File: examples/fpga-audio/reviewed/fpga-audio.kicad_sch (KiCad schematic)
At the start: 36 parts, among them J1 3V3 IN, J2 AUDIO OUT, J3 SPI PROG, U1 iCE40UP5K, U2 PCM5102A, U3 AP2112K-1.2, U4 W25Q32JV, X1 12MHz

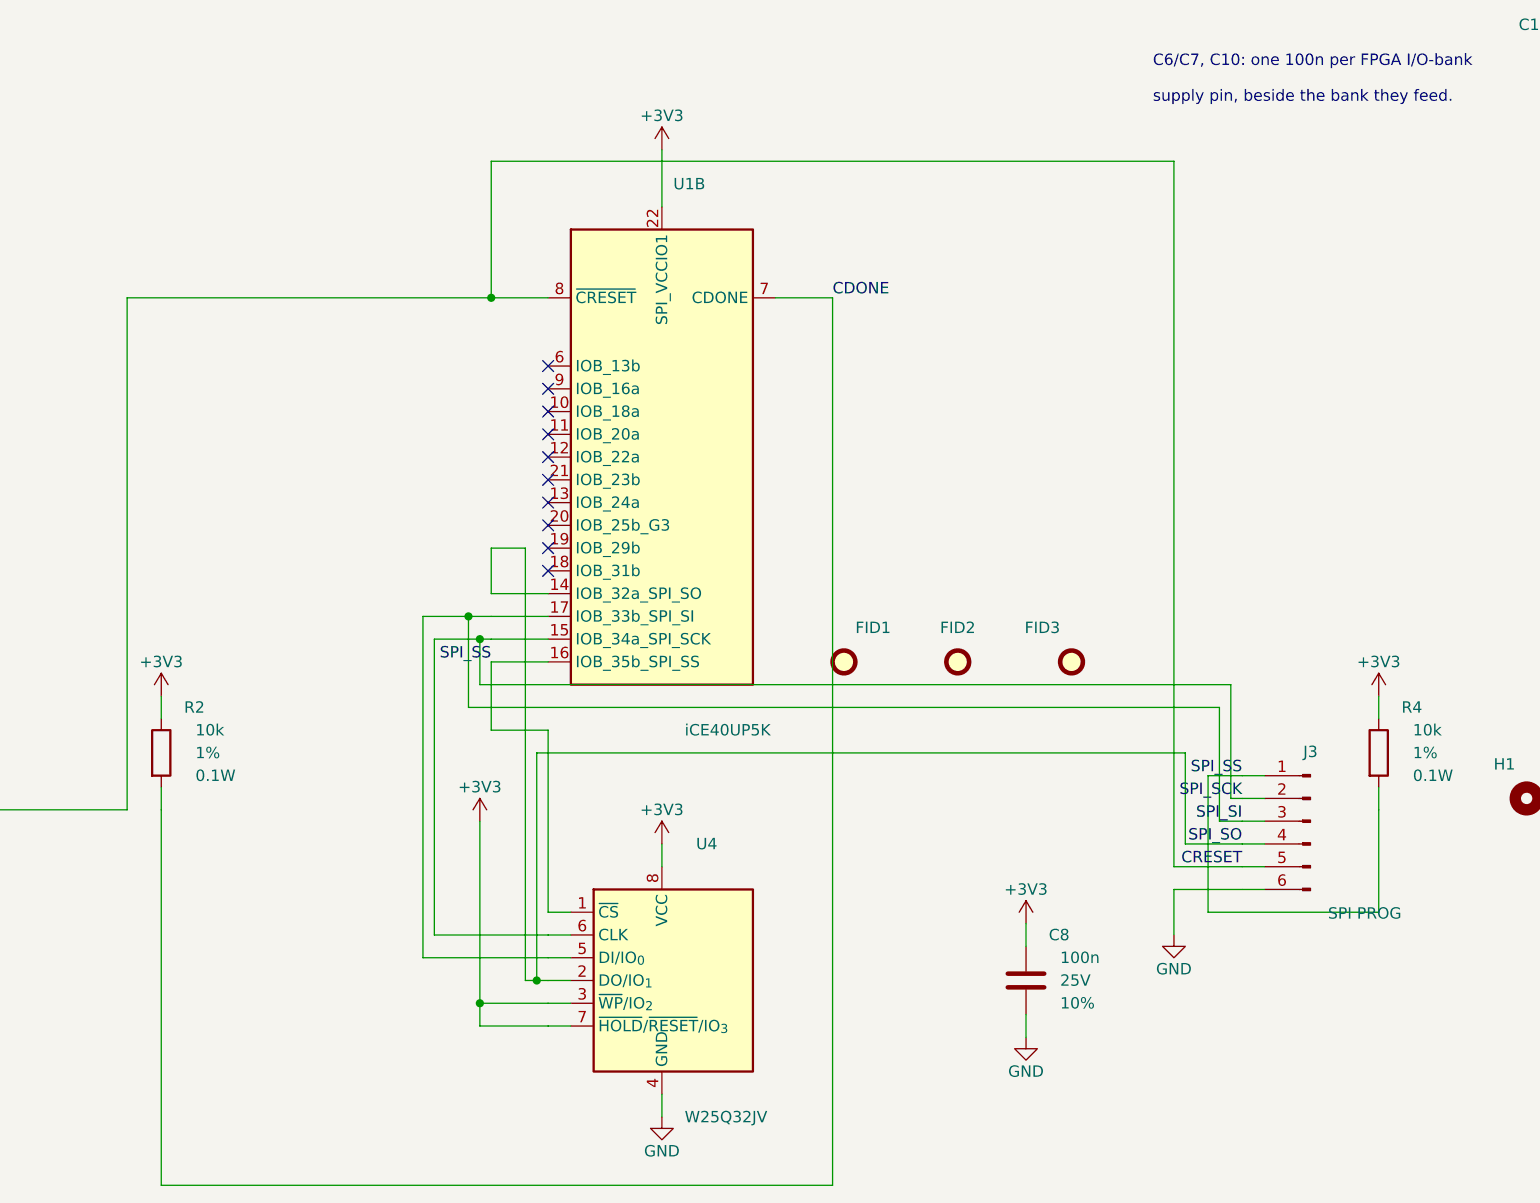
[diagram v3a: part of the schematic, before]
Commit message: Walk the whole edge for a screw hole, and land a joint on its own pad
The fastener clearance was right and the search was not: it slid along two
edges from each corner and gave up, so boards that had had four screw holes
came back with one. It now walks a ring round the board at the inset the
screw needs, taking the nearest free point to each corner - and only from
that corner's own quarter, because a search that asked for the nearest free
point anywhere put three of the four along one edge, each of them the nearest
thing to a different corner. A quarter with no room gives no screw: three
that hold the board flat beat four that hold one side.

A pin header asks for nothing above its courtyard - the socket that fits it
lands inside the outline the header already draws - while a screw terminal's
wires leave horizontally from its face. Treating the two alike is what left a
carrier lined with headers with two holes on one edge. Both the generator and
the rule now tell them apart by footprint.

_landed folds a via that sits beside a plated hole of its own net onto the
hole. The plating already joins the faces, so the via bought nothing and cost
hole-to-hole: two drills a millimetre apart leave 0.15 mm of laminate at a
0.25 mm rule, which is what DRC reported on the opamp board.

The fillets move to the end of the pipeline. A taper is built against the end
of a run, and _landed moves ends, so a teardrop laid before it pointed at
where the run used to stop - a nought-degree corner in the angle rule.

buck-5v, motor-driver, pico-carrier, opamp-filter: 0 errors, 0 warnings.

Co-Authored-By: Claude Fable 5 <noreply@anthropic.com>
Claude-Session: https://claude.ai/code/session_01DUj7Ltu92tWg159mCSacwY
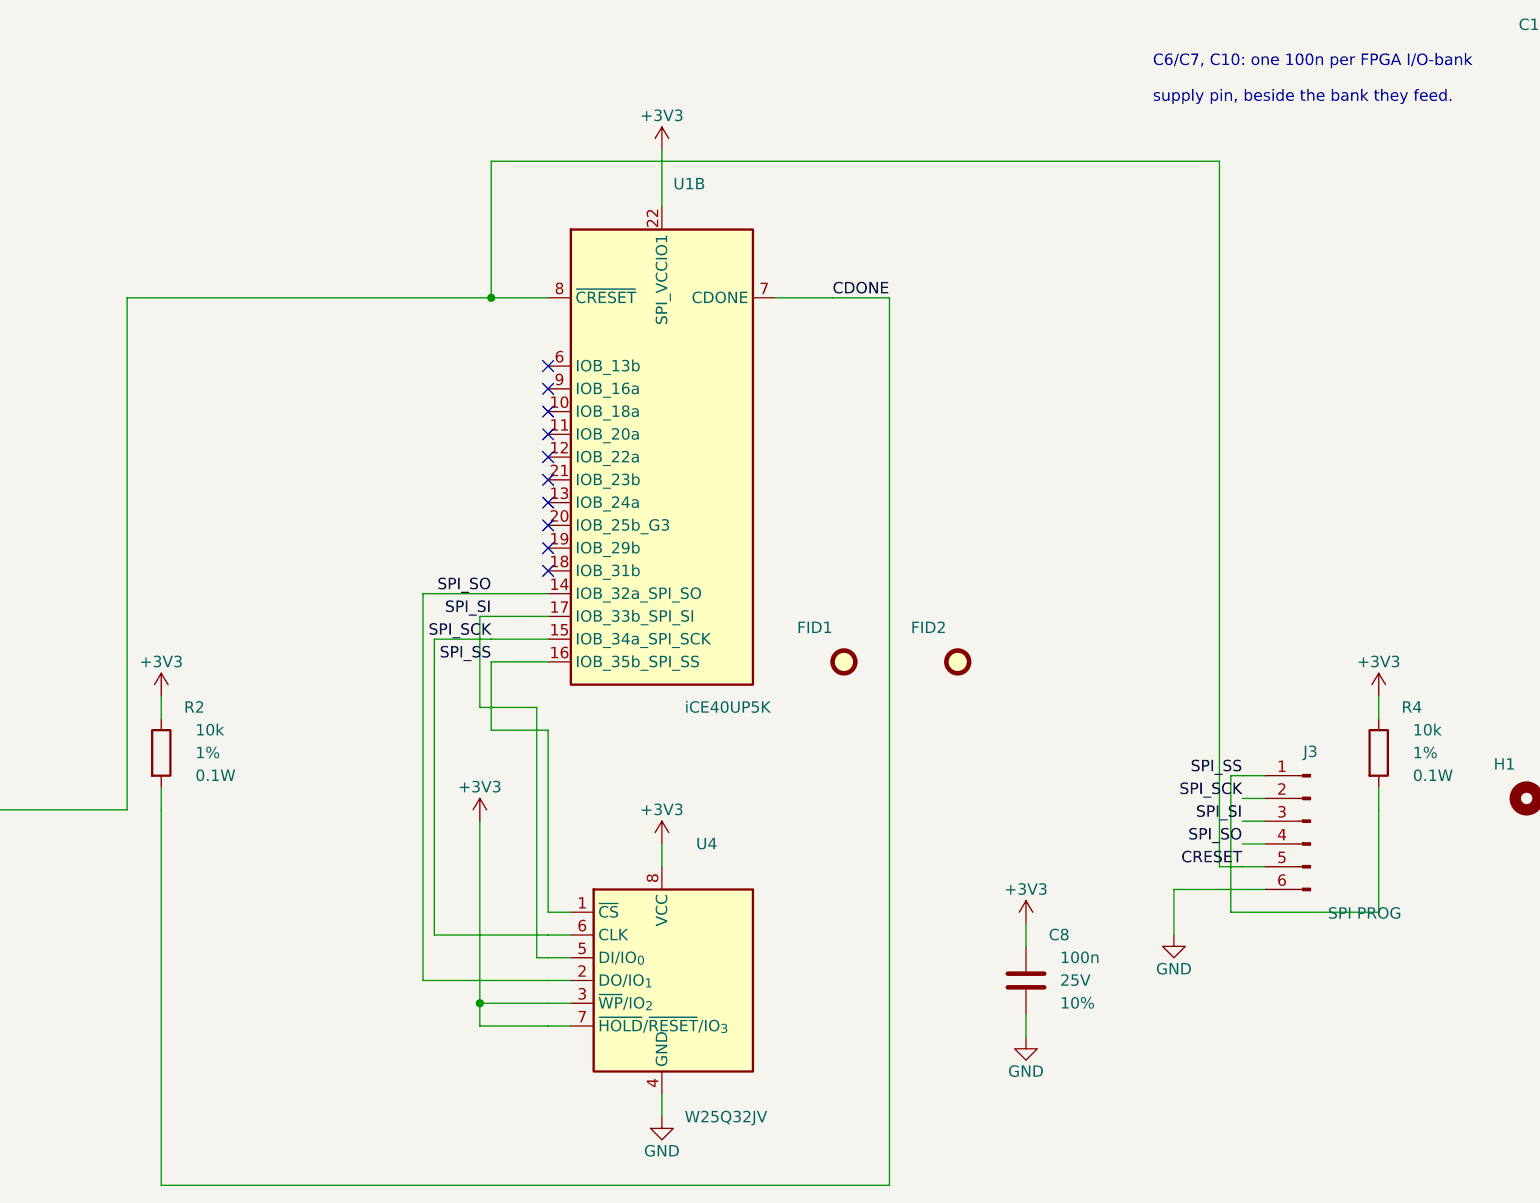
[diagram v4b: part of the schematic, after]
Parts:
- removed FID3: Fiducial, Fiducial:Fiducial_1mm_Mask2mm, symbol Mechanical:Fiducial
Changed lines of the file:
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@@
   (wire (pts (xy 180.34 22.86) (xy 180.34 41.91)) (stroke (width 0) (type default)))
   (wire (pts (xy 114.3 22.86) (xy 180.34 22.86)) (stroke (width 0) (type default)))
-  (wire (pts (xy 170.18 219.71) (xy 175.26 219.71)) (stroke (width 0) (type default)))
-  (wire (pts (xy 175.26 219.71) (xy 176.53 219.71)) (stroke (width 0) (type default)))
+  (wire (pts (xy 170.18 219.71) (xy 176.53 219.71)) (stroke (width 0) (type default)))
   (wire (pts (xy 170.18 219.71) (xy 170.18 252.73)) (stroke (width 0) (type default)))
   (wire (pts (xy 170.18 252.73) (xy 182.88 252.73)) (stroke (width 0) (type default)))
-  (wire (pts (xy 175.26 219.71) (xy 175.26 224.79)) (stroke (width 0) (type default)))
-  (wire (pts (xy 175.26 224.79) (xy 259.08 224.79)) (stroke (width 0) (type default)))
-  (wire (pts (xy 259.08 224.79) (xy 259.08 237.49)) (stroke (width 0) (type default)))
-  (wire (pts (xy 259.08 237.49) (xy 260.35 237.49)) (stroke (width 0) (type default)))
-  (wire (pts (xy 168.91 217.17) (xy 173.99 217.17)) (stroke (width 0) (type default)))
-  (wire (pts (xy 173.99 217.17) (xy 176.53 217.17)) (stroke (width 0) (type default)))
-  (wire (pts (xy 168.91 217.17) (xy 168.91 255.27)) (stroke (width 0) (type default)))
-  (wire (pts (xy 168.91 255.27) (xy 182.88 255.27)) (stroke (width 0) (type default)))
-  (wire (pts (xy 173.99 217.17) (xy 173.99 227.33)) (stroke (width 0) (type default)))
-  (wire (pts (xy 173.99 227.33) (xy 257.81 227.33)) (stroke (width 0) (type default)))
-  (wire (pts (xy 257.81 227.33) (xy 257.81 240.03)) (stroke (width 0) (type default)))
-  (wire (pts (xy 257.81 240.03) (xy 260.35 240.03)) (stroke (width 0) (type default)))
+  (wire (pts (xy 175.26 217.17) (xy 176.53 217.17)) (stroke (width 0) (type default)))
+  (wire (pts (xy 175.26 217.17) (xy 175.26 227.33)) (stroke (width 0) (type default)))
+  (wire (pts (xy 175.26 227.33) (xy 181.61 227.33)) (stroke (width 0) (type default)))
+  (wire (pts (xy 181.61 227.33) (xy 181.61 255.27)) (stroke (width 0) (type default)))
+  (wire (pts (xy 181.61 255.27) (xy 182.88 255.27)) (stroke (width 0) (type default)))
   (wire (pts (xy 176.53 222.25) (xy 176.53 229.87)) (stroke (width 0) (type default)))
   (wire (pts (xy 176.53 229.87) (xy 182.88 229.87)) (stroke (width 0) (type default)))
   (wire (pts (xy 182.88 229.87) (xy 182.88 250.19)) (stroke (width 0) (type default)))
-  (wire (pts (xy 256.54 234.95) (xy 260.35 234.95)) (stroke (width 0) (type default)))
-  (wire (pts (xy 256.54 234.95) (xy 256.54 250.19)) (stroke (width 0) (type default)))
-  (wire (pts (xy 256.54 250.19) (xy 275.59 250.19)) (stroke (width 0) (type default)))
+  (wire (pts (xy 259.08 234.95) (xy 260.35 234.95)) (stroke (width 0) (type default)))
+  (wire (pts (xy 259.08 234.95) (xy 259.08 250.19)) (stroke (width 0) (type default)))
+  (wire (pts (xy 259.08 250.19) (xy 275.59 250.19)) (stroke (width 0) (type default)))
   (wire (pts (xy 275.59 238.76) (xy 275.59 250.19)) (stroke (width 0) (type default)))
-  (wire (pts (xy 176.53 209.55) (xy 176.53 214.63)) (stroke (width 0) (type default)))
-  (wire (pts (xy 176.53 209.55) (xy 180.34 209.55)) (stroke (width 0) (type default)))
-  (wire (pts (xy 180.34 209.55) (xy 180.34 257.81)) (stroke (width 0) (type default)))
-  (wire (pts (xy 180.34 257.81) (xy 181.61 257.81)) (stroke (width 0) (type default)))
-  (wire (pts (xy 181.61 257.81) (xy 182.88 257.81)) (stroke (width 0) (type default)))
-  (wire (pts (xy 181.61 232.41) (xy 181.61 257.81)) (stroke (width 0) (type default)))
-  (wire (pts (xy 181.61 232.41) (xy 254.0 232.41)) (stroke (width 0) (type default)))
-  (wire (pts (xy 254.0 232.41) (xy 254.0 242.57)) (stroke (width 0) (type default)))
-  (wire (pts (xy 254.0 242.57) (xy 260.35 242.57)) (stroke (width 0) (type default)))
-  (wire (pts (xy 214.63 181.61) (xy 214.63 280.67)) (stroke (width 0) (type default)))
-  (wire (pts (xy 139.7 280.67) (xy 214.63 280.67)) (stroke (width 0) (type default)))
+  (wire (pts (xy 168.91 214.63) (xy 176.53 214.63)) (stroke (width 0) (type default)))
+  (wire (pts (xy 168.91 214.63) (xy 168.91 257.81)) (stroke (width 0) (type default)))
+  (wire (pts (xy 168.91 257.81) (xy 182.88 257.81)) (stroke (width 0) (type default)))
+  (wire (pts (xy 214.63 181.61) (xy 220.98 181.61)) (stroke (width 0) (type default)))
+  (wire (pts (xy 220.98 181.61) (xy 220.98 280.67)) (stroke (width 0) (type default)))
+  (wire (pts (xy 139.7 280.67) (xy 220.98 280.67)) (stroke (width 0) (type default)))
   (wire (pts (xy 139.7 238.76) (xy 139.7 280.67)) (stroke (width 0) (type default)))
   (wire (pts (xy 66.04 36.83) (xy 72.39 36.83)) (stroke (width 0) (type default)))
@@
   (wire (pts (xy 111.76 238.76) (xy 135.89 238.76)) (stroke (width 0) (type default)))
   (wire (pts (xy 176.53 166.37) (xy 176.53 181.61)) (stroke (width 0) (type default)))
-  (wire (pts (xy 176.53 166.37) (xy 252.73 166.37)) (stroke (width 0) (type default)))
-  (wire (pts (xy 252.73 166.37) (xy 252.73 245.11)) (stroke (width 0) (type default)))
-  (wire (pts (xy 252.73 245.11) (xy 260.35 245.11)) (stroke (width 0) (type default)))
+  (wire (pts (xy 176.53 166.37) (xy 257.81 166.37)) (stroke (width 0) (type default)))
+  (wire (pts (xy 257.81 166.37) (xy 257.81 245.11)) (stroke (width 0) (type default)))
+  (wire (pts (xy 257.81 245.11) (xy 260.35 245.11)) (stroke (width 0) (type default)))
   (junction (at 66.04 36.83) (diameter 0) (color 0 0 0 0))
   (junction (at 163.83 41.91) (diameter 0) (color 0 0 0 0))
-  (junction (at 173.99 217.17) (diameter 0) (color 0 0 0 0))
-  (junction (at 175.26 219.71) (diameter 0) (color 0 0 0 0))
   (junction (at 176.53 181.61) (diameter 0) (color 0 0 0 0))
   (junction (at 180.34 41.91) (diameter 0) (color 0 0 0 0))
-  (junction (at 181.61 257.81) (diameter 0) (color 0 0 0 0))
   (no_connect (at 185.42 95.25))
   (no_connect (at 185.42 97.79))
@@
   (no_connect (at 182.88 212.09))
   (wire (pts (xy 182.88 214.63) (xy 176.53 214.63)) (stroke (width 0) (type default)))
+  (label "SPI_SO" (at 176.53 214.63 0) (effects (font (size 1.27 1.27)) (justify right bottom)))
   (wire (pts (xy 182.88 217.17) (xy 176.53 217.17)) (stroke (width 0) (type default)))
+  (label "SPI_SI" (at 176.53 217.17 0) (effects (font (size 1.27 1.27)) (justify right bottom)))
   (wire (pts (xy 182.88 219.71) (xy 176.53 219.71)) (stroke (width 0) (type default)))
+  (label "SPI_SCK" (at 176.53 219.71 0) (effects (font (size 1.27 1.27)) (justify right bottom)))
   (wire (pts (xy 182.88 222.25) (xy 176.53 222.25)) (stroke (width 0) (type default)))
   (label "SPI_SS" (at 176.53 222.25 0) (effects (font (size 1.27 1.27)) (justify right bottom)))
@@
     (exclude_from_sim no) (in_bom yes) (on_board yes) (dnp no)
     (property "Reference" "U1" (at 196.85 168.91 0) (effects (font (size 1.27 1.27)) (justify left)))
-    (property "Value" "iCE40UP5K" (at 198.12 229.87 0) (effects (font (size 1.27 1.27)) (justify left)))
+    (property "Value" "iCE40UP5K" (at 198.12 227.33 0) (effects (font (size 1.27 1.27)) (justify left)))
     (property "Footprint" "Package_DFN_QFN:QFN-48-1EP_7x7mm_P0.5mm_EP3.5x3.5mm" (at 195.58 199.39 0) (effects (font (size 1.27 1.27)) hide))
     (property "Datasheet" "https://www.latticesemi.com/view_document?document_id=51968" (at 195.58 199.39 0) (effects (font (size 1.27 1.27)) hide))
@@
   (symbol (lib_id "Mechanical:Fiducial") (at 215.9 222.25 0.0) (unit 1)
     (exclude_from_sim no) (in_bom no) (on_board yes) (dnp no)
-    (property "Reference" "FID1" (at 217.17 218.44 0) (effects (font (size 1.27 1.27)) (justify left)))
-    (property "Value" "Fiducial" (at 217.17 229.87 0) (effects (font (size 1.27 1.27)) (justify left) hide))
+    (property "Reference" "FID1" (at 214.63 218.44 0) (effects (font (size 1.27 1.27)) (justify right)))
+    (property "Value" "Fiducial" (at 212.09 224.79 0) (effects (font (size 1.27 1.27)) (justify right) hide))
     (property "Footprint" "Fiducial:Fiducial_1mm_Mask2mm" (at 215.9 222.25 0) (effects (font (size 1.27 1.27)) hide))
     (property "Datasheet" "~" (at 215.9 222.25 0) (effects (font (size 1.27 1.27)) hide))
@@
   (symbol (lib_id "Mechanical:Fiducial") (at 228.6 222.25 0.0) (unit 1)
     (exclude_from_sim no) (in_bom no) (on_board yes) (dnp no)
-    (property "Reference" "FID2" (at 228.6 218.44 0) (effects (font (size 1.27 1.27))))
-    (property "Value" "Fiducial" (at 229.87 229.87 0) (effects (font (size 1.27 1.27)) (justify left) hide))
+    (property "Reference" "FID2" (at 227.33 218.44 0) (effects (font (size 1.27 1.27)) (justify right)))
+    (property "Value" "Fiducial" (at 232.41 224.79 0) (effects (font (size 1.27 1.27)) (justify left) hide))
     (property "Footprint" "Fiducial:Fiducial_1mm_Mask2mm" (at 228.6 222.25 0) (effects (font (size 1.27 1.27)) hide))
     (property "Datasheet" "~" (at 228.6 222.25 0) (effects (font (size 1.27 1.27)) hide))
@@
     (instances (project "fpga-audio" (path "/434dea94-d96f-5288-b60c-67317d440f4e" (reference "FID2") (unit 1))))
   )
-  (symbol (lib_id "Mechanical:Fiducial") (at 241.3 222.25 0.0) (unit 1)
-    (exclude_from_sim no) (in_bom no) (on_board yes) (dnp no)
-    (property "Reference" "FID3" (at 240.03 218.44 0) (effects (font (size 1.27 1.27)) (justify right)))
-    (property "Value" "Fiducial" (at 237.49 224.79 0) (effects (font (size 1.27 1.27)) (justify right) hide))
-    (property "Footprint" "Fiducial:Fiducial_1mm_Mask2mm" (at 241.3 222.25 0) (effects (font (size 1.27 1.27)) hide))
-    (property "Datasheet" "~" (at 241.3 222.25 0) (effects (font (size 1.27 1.27)) hide))
-    (property "MPN" "n/a" (at 241.3 222.25 0) (effects (font (size 1.27 1.27)) hide))
-    (property "Manufacturer" "n/a" (at 241.3 222.25 0) (effects (font (size 1.27 1.27)) hide))
-    (instances (project "fpga-audio" (path "/434dea94-d96f-5288-b60c-67317d440f4e" (reference "FID3") (unit 1))))
-  )
   (wire (pts (xy 311.15 118.11) (xy 303.53 118.11)) (stroke (width 0) (type default)))

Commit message: Move the corner that belongs to neither track
route.acute_angle reads copper, not the objects the copper was written from,
so it sees two corners no pass could: a joint where a run of one width meets a
run of another, and a pair of segments eighteen microns long left by a chamfer
of a chamfer - an 88 degree corner on a run that is visibly straight.

_welded takes both. The debris comes out where a point has debris on each side,
so a genuinely short leg into a pad keeps its shape. The joint moves: the two
far ends stay put and the point between them becomes the elbow that joins them
without reversing, each track keeping one leg and its own width.

_pinned_points is deliberately not what holds a joint still - that set pins
every track end, because moving one of a pair leaves the other in mid air,
which is the case this pass exists for and handles by moving both. What may
not move is a pad or a via.

fpga-audio is down to two: three nets over cuts in the plane, and one run that
tours. The other four stay at 0 errors, 0 warnings.

Co-Authored-By: Claude Fable 5 <noreply@anthropic.com>
Claude-Session: https://claude.ai/code/session_01DUj7Ltu92tWg159mCSacwY
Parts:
- added FID3: Fiducial, Fiducial:Fiducial_1mm_Mask2mm, symbol Mechanical:Fiducial
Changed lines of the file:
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@@
     (instances (project "fpga-audio" (path "/434dea94-d96f-5288-b60c-67317d440f4e" (reference "FID2") (unit 1))))
+  )
+  (symbol (lib_id "Mechanical:Fiducial") (at 241.3 222.25 0.0) (unit 1)
+    (exclude_from_sim no) (in_bom no) (on_board yes) (dnp no)
+    (property "Reference" "FID3" (at 240.03 218.44 0) (effects (font (size 1.27 1.27)) (justify right)))
+    (property "Value" "Fiducial" (at 245.11 224.79 0) (effects (font (size 1.27 1.27)) (justify left) hide))
+    (property "Footprint" "Fiducial:Fiducial_1mm_Mask2mm" (at 241.3 222.25 0) (effects (font (size 1.27 1.27)) hide))
+    (property "Datasheet" "~" (at 241.3 222.25 0) (effects (font (size 1.27 1.27)) hide))
+    (property "MPN" "n/a" (at 241.3 222.25 0) (effects (font (size 1.27 1.27)) hide))
+    (property "Manufacturer" "n/a" (at 241.3 222.25 0) (effects (font (size 1.27 1.27)) hide))
+    (instances (project "fpga-audio" (path "/434dea94-d96f-5288-b60c-67317d440f4e" (reference "FID3") (unit 1))))
   )
   (wire (pts (xy 311.15 118.11) (xy 303.53 118.11)) (stroke (width 0) (type default)))
